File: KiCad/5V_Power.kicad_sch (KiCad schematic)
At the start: 12 parts, among them J4 USB_C_Receptacle_USB2.0_14P

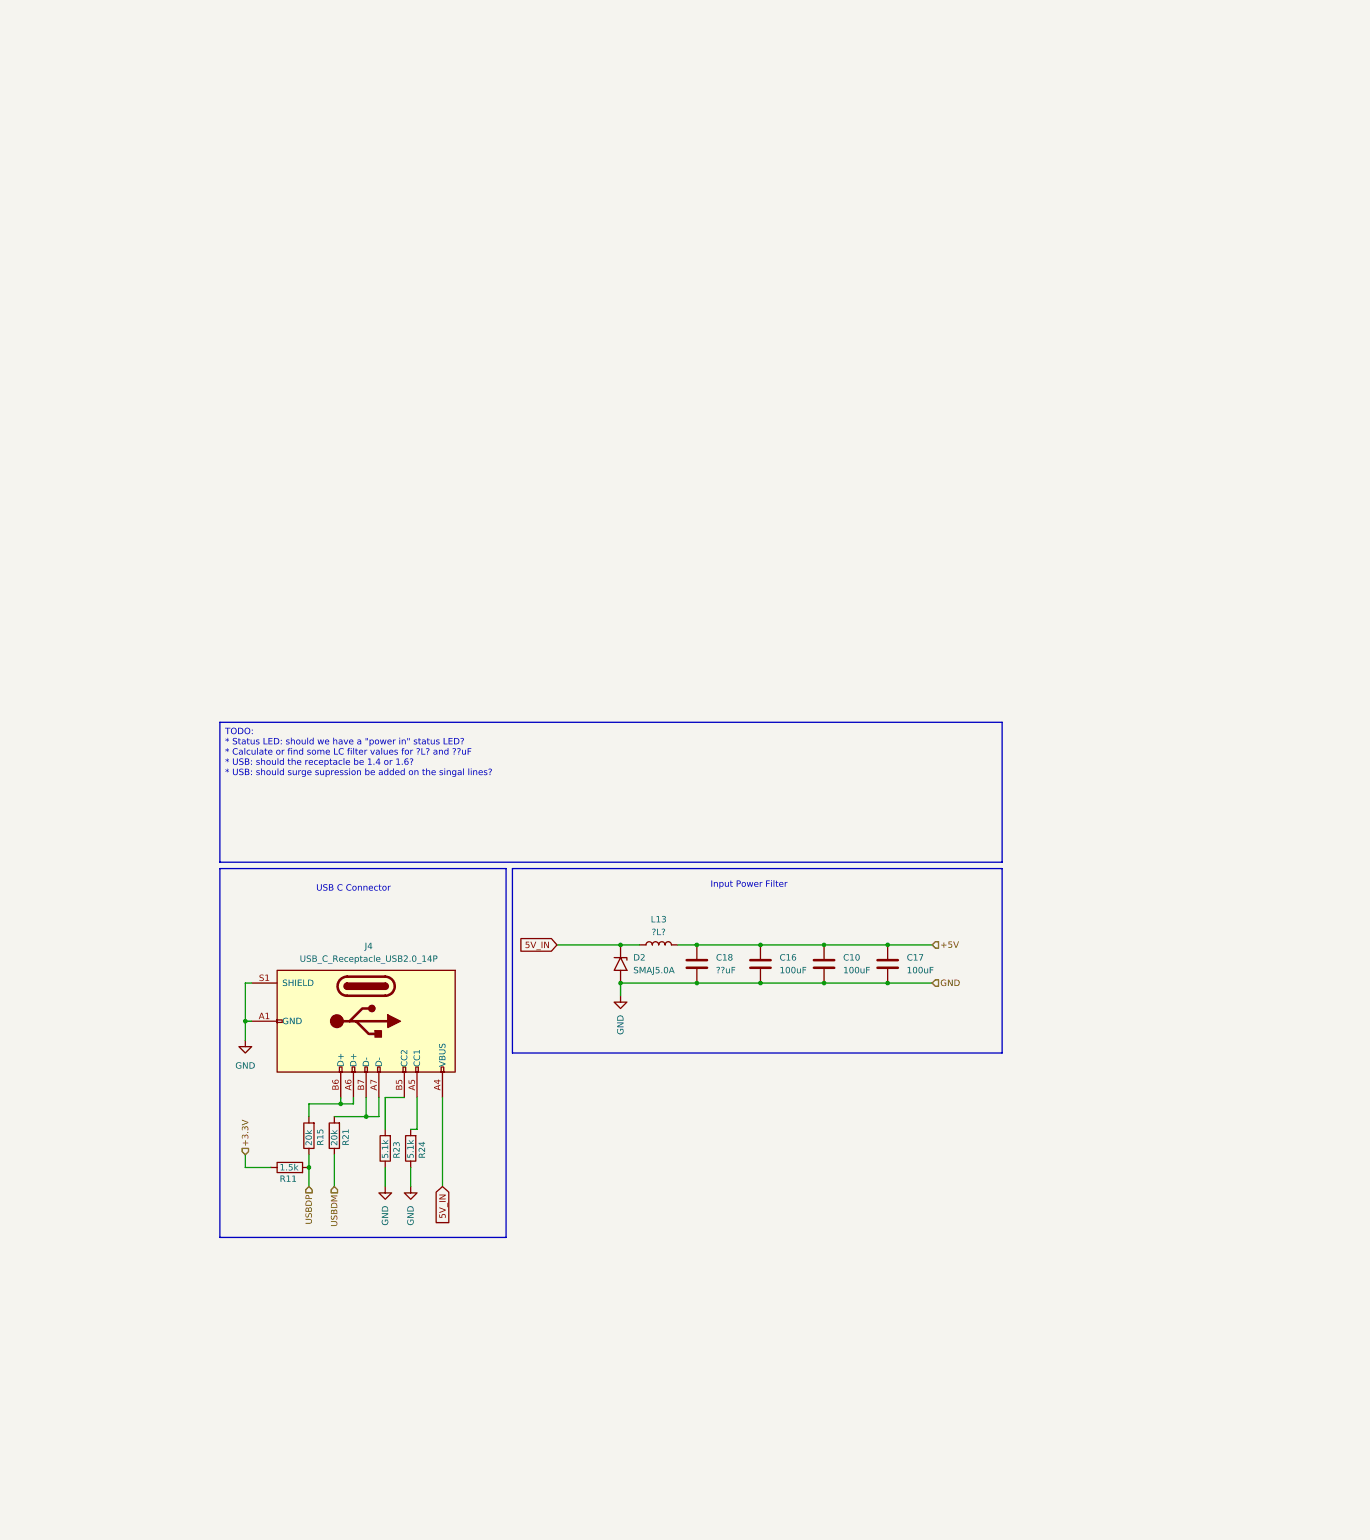
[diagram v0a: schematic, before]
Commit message: Use 12V Power
* Use 12 V Power
* Update to an F103 processor with better compatibility with Katapult
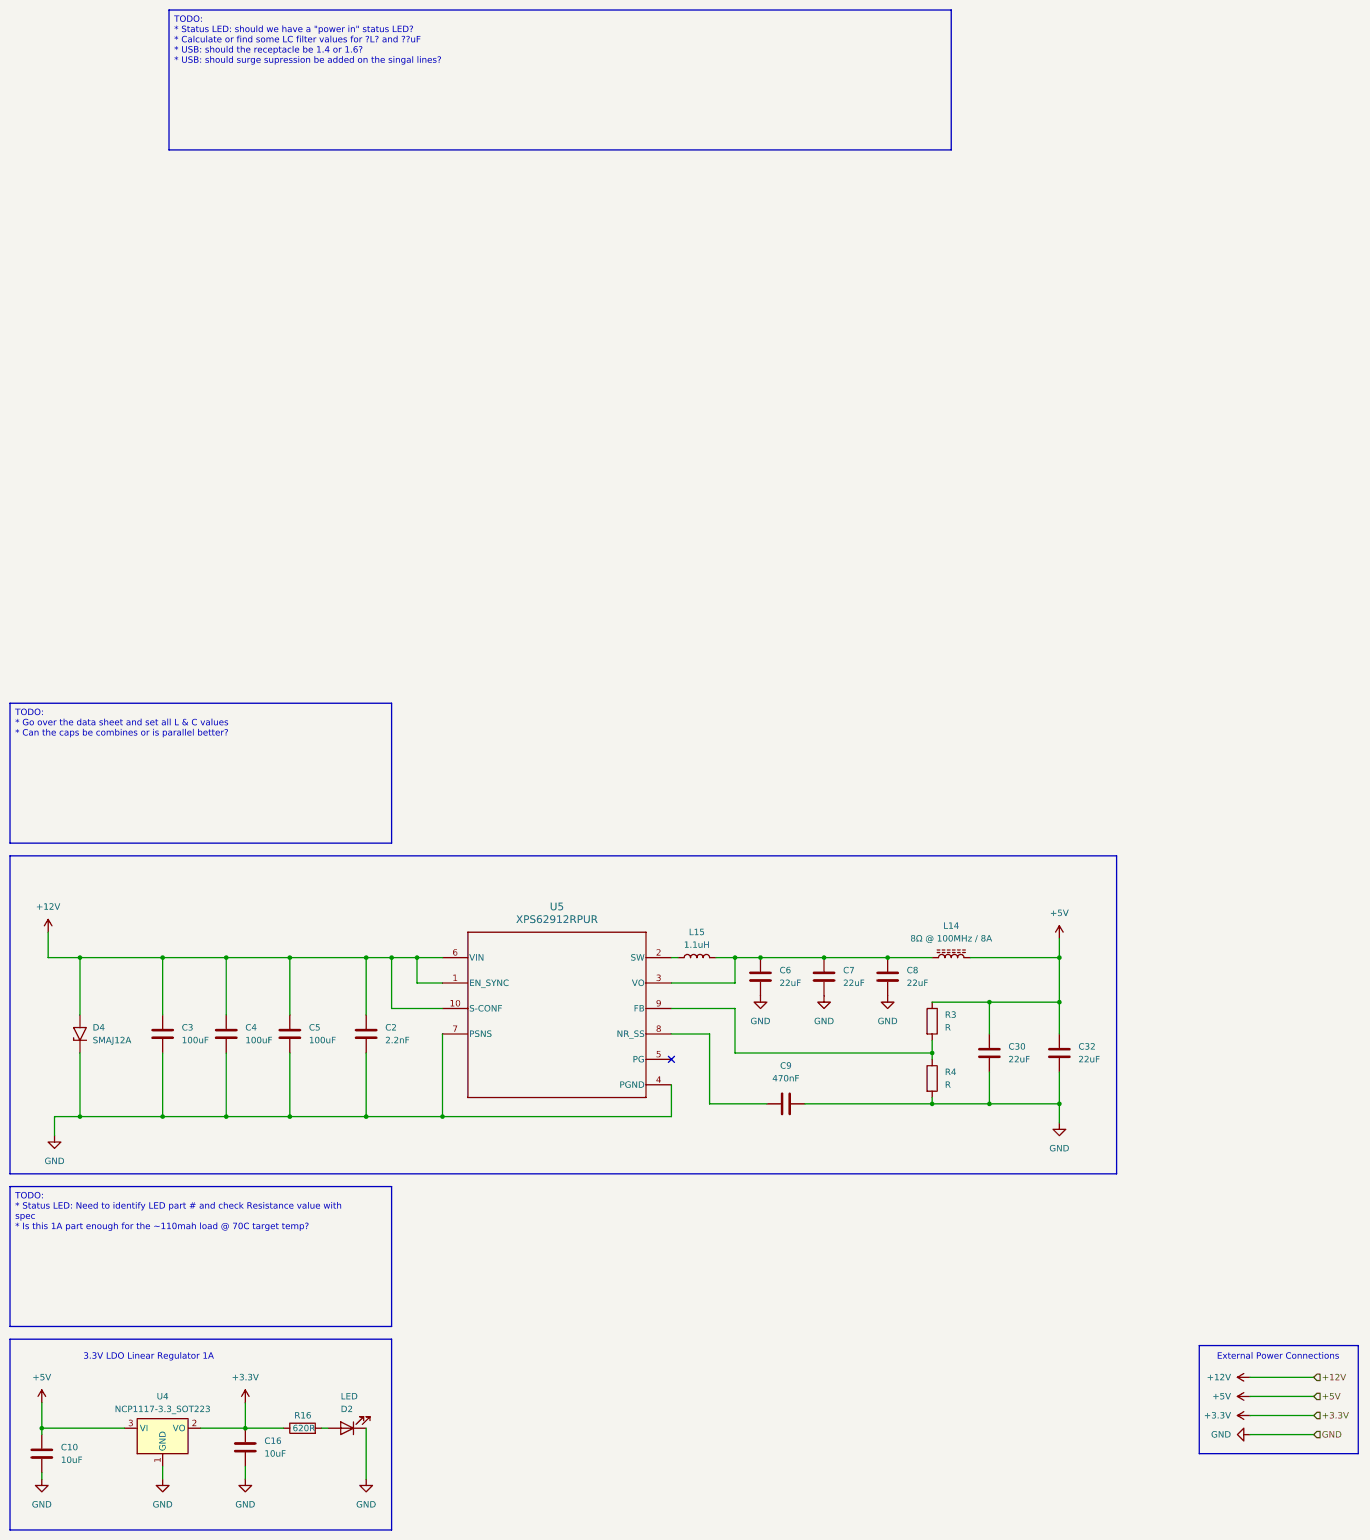
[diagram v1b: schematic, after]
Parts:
- removed C17: 100uF, symbol Device:C
- removed C18: ??uF, symbol Device:C
- removed D2: SMAJ5.0A, Diode_SMD:D_SMA, symbol Diode:SMAJ5.0A
- removed J4: USB_C_Receptacle_USB2.0_14P, symbol Connector:USB_C_Receptacle_USB2.0_14P
- removed L13: ?L?, symbol Device:L
- removed R11: 1.5k, symbol Device:R
- removed R15, R21: 20k, symbol Device:R
- removed R23, R24: 5.1k, symbol Device:R
- added C2: 2.2nF, Capacitor_SMD:C_0603_1608Metric_Pad1.08x0.95mm_HandSolder, symbol Device:C
- added C3, C4, C5: 100uF, Capacitor_SMD:C_1206_3216Metric, symbol Device:C
- added C30, C32, C6, C7, C8: 22uF, Capacitor_SMD:C_0603_1608Metric_Pad1.08x0.95mm_HandSolder, symbol Device:C
- added C9: 470nF, Capacitor_SMD:C_0603_1608Metric_Pad1.08x0.95mm_HandSolder, symbol Device:C
- added D2: LED, LED_SMD:LED_1206_3216Metric_Pad1.42x1.75mm_HandSolder, symbol Device:LED
- added D4: SMAJ12A, Diode_SMD:D_SMA, symbol Diode:SMAJ12A
- added L14: 8Ω @ 100MHz / 8A, Inductor_SMD:L_0603_1608Metric_Pad1.05x0.95mm_HandSolder, symbol Device:L_Ferrite
- added L15: 1.1uH, Capacitor_SMD:C_0603_1608Metric_Pad1.08x0.95mm_HandSolder, symbol Device:L
- added R16: 620R, Resistor_SMD:R_0603_1608Metric_Pad0.98x0.95mm_HandSolder, symbol Device:R
- added R3, R4: R, Resistor_SMD:R_0603_1608Metric_Pad0.98x0.95mm_HandSolder, symbol Device:R
- added U4: NCP1117-3.3_SOT223, Package_TO_SOT_SMD:SOT-223-3_TabPin2, symbol Regulator_Linear:NCP1117-3.3_SOT223
- added U5: XPS62912RPUR, RPU0010A-MFG, symbol TPS62912:XPS62912RPUR
- C10, C16: value 100uF -> 10uF; footprint (none) -> Capacitor_SMD:C_0603_1608Metric_Pad1.08x0.95mm_HandSolder
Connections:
- net +3.3V: now also C16.1, R16.1, U4.2 (VO)
- net +5V: now also C30.1, C32.1, L14.2, R3.1, U4.3 (VI); no longer C16.1
- net GND: now also C2.2, C3.2, C30.2, C32.2, C4.2, C5.2, C6.2, C7.2, C8.2, C9.1, D2.1 (K), D4.1 (A1), R4.2, U4.1 (GND), U5.4 (PGND), U5.7 (PSNS)
- new net: D2.2 (A), R16.2
- new net: C6.1, C7.1, C8.1, L14.1, L15.2, U5.3 (VO)
- new net: L15.1, U5.2 (SW)
- new net: C9.2, U5.8 (NR_SS)
- new net: R3.2, R4.1, U5.9 (FB)
- new net +12V: C2.1, C3.1, C4.1, C5.1, D4.2 (A2), U5.1 (EN_SYNC), U5.10 (S-CONF), U5.6 (VIN)
- no-connect marks 0 -> 1
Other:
- note added: "3.3V LDO Linear Regulator 1A"
- note added: "External Power Connections"
- note removed: "Input Power Filter"
- note removed: "USB C Connector"

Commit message: Update 5V Power Stage
* Update the 5V power stage based on the recommendations from TI.
* Updated standard passive footprint to 0805 hand solder configuration
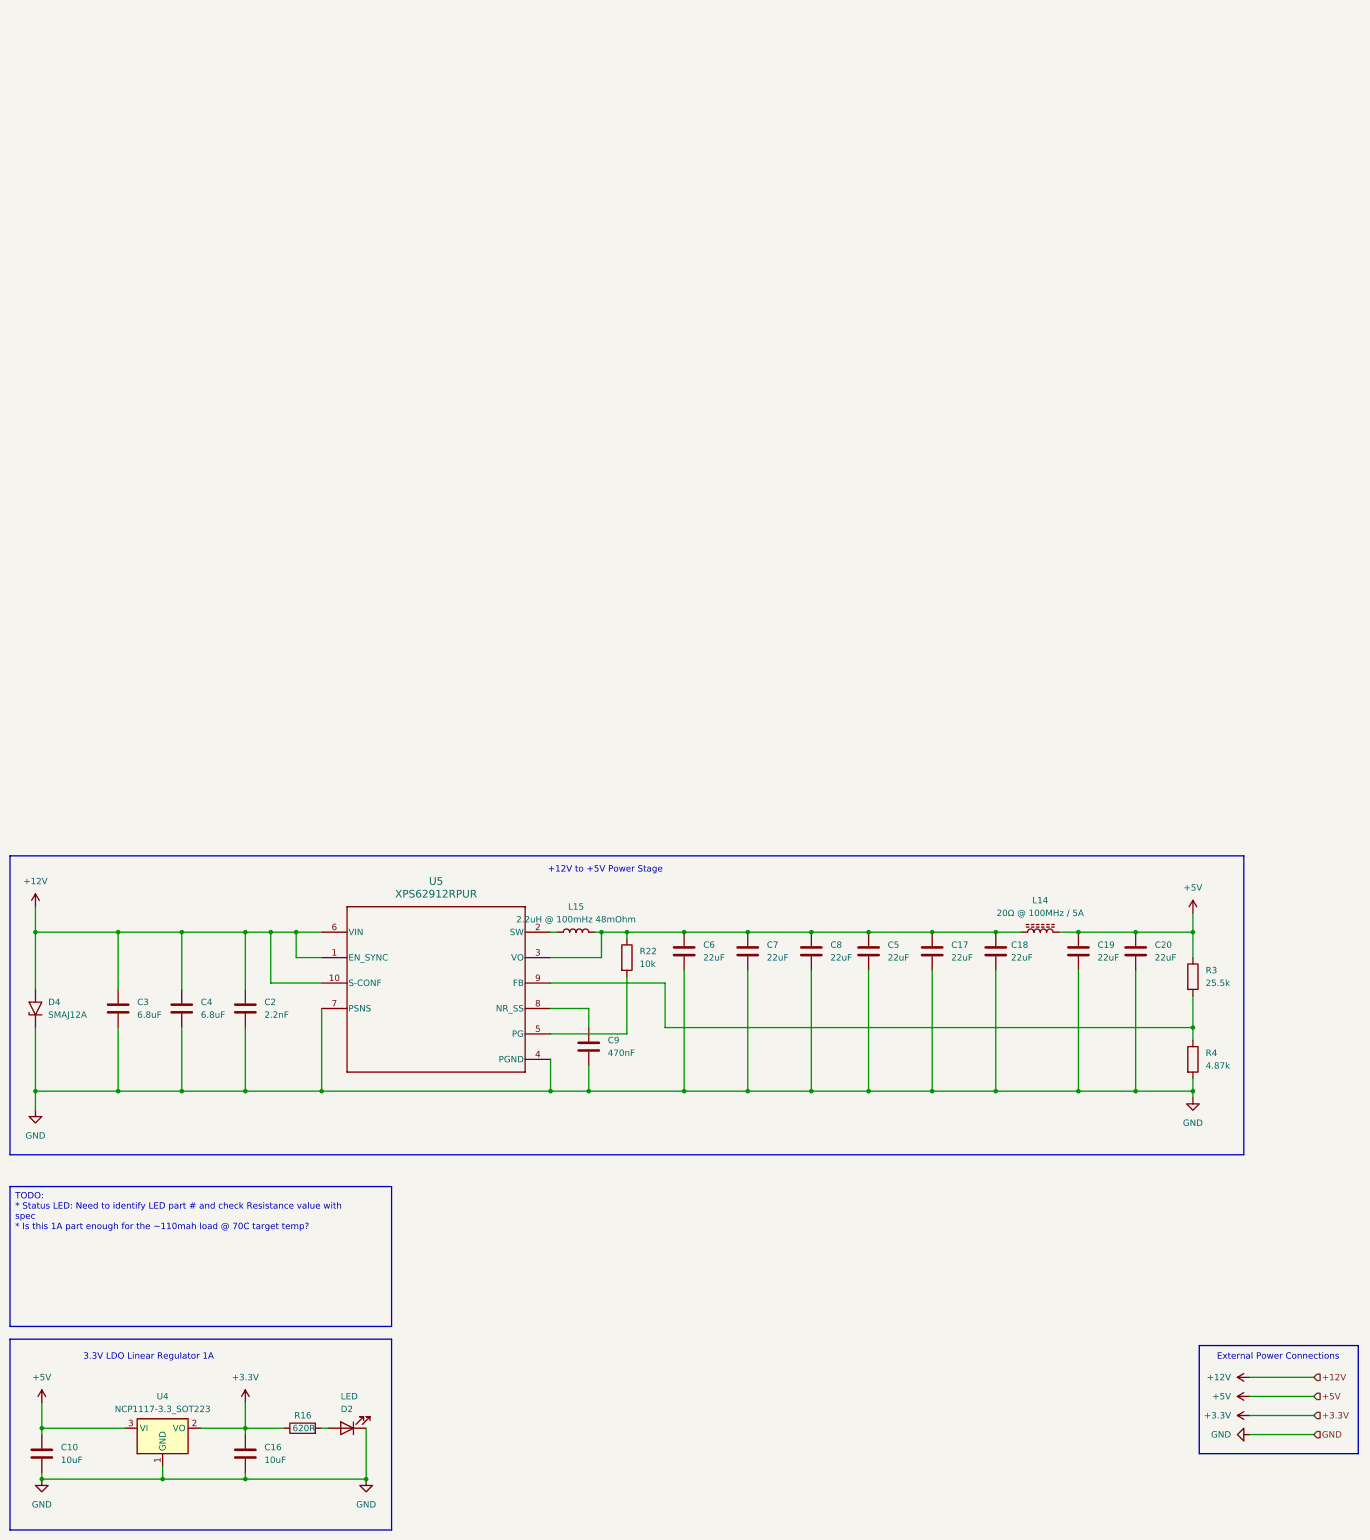
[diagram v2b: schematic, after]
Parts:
- removed C30, C32: 22uF, Capacitor_SMD:C_0603_1608Metric_Pad1.08x0.95mm_HandSolder, symbol Device:C
- added C17, C18, C19, C20: 22uF, Capacitor_SMD:C_0805_2012Metric_Pad1.18x1.45mm_HandSolder, symbol Device:C
- added R22: 10k, Resistor_SMD:R_0805_2012Metric_Pad1.20x1.40mm_HandSolder, symbol Device:R
- C10, C16, C2, C6, C7, C8, C9: footprint Capacitor_SMD:C_0603_1608Metric_Pad1.08x0.95mm_HandSolder -> Capacitor_SMD:C_0805_2012Metric_Pad1.18x1.45mm_HandSolder
- C3, C4: value 100uF -> 6.8uF; footprint Capacitor_SMD:C_1206_3216Metric -> Capacitor_SMD:C_0805_2012Metric_Pad1.18x1.45mm_HandSolder
- C5: value 100uF -> 22uF; footprint Capacitor_SMD:C_1206_3216Metric -> Capacitor_SMD:C_0805_2012Metric_Pad1.18x1.45mm_HandSolder
- L14: value 8Ω @ 100MHz / 8A -> 20Ω @ 100MHz / 5A; footprint Inductor_SMD:L_0603_1608Metric_Pad1.05x0.95mm_HandSolder -> Inductor_SMD:L_0805_2012Metric_Pad1.05x1.20mm_HandSolder
- L15: value 1.1uH -> 2.2uH @ 100mHz 48mOhm; footprint Capacitor_SMD:C_0603_1608Metric_Pad1.08x0.95mm_HandSolder -> Inductor_SMD:L_Pulse_PA4320
- R16: footprint Resistor_SMD:R_0603_1608Metric_Pad0.98x0.95mm_HandSolder -> Resistor_SMD:R_0805_2012Metric_Pad1.20x1.40mm_HandSolder
- R3: value R -> 25.5k; footprint Resistor_SMD:R_0603_1608Metric_Pad0.98x0.95mm_HandSolder -> Resistor_SMD:R_0805_2012Metric_Pad1.20x1.40mm_HandSolder
- R4: value R -> 4.87k; footprint Resistor_SMD:R_0603_1608Metric_Pad0.98x0.95mm_HandSolder -> Resistor_SMD:R_0805_2012Metric_Pad1.20x1.40mm_HandSolder
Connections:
- net +12V: no longer C5.1
- net +5V: now also C19.1, C20.1
- net GND: now also C17.2, C18.2, C19.2, C20.2
- net at C6.1, C7.1, C8.1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: now also C5.1, C17.1, C18.1, R22.1
- net at U5.5 (PG): now also R22.2
- no-connect marks 1 -> 0
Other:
- note added: "+12V to +5V Power Stage"
- moved on the sheet: C16, C2, C3, C4, C6, C7, C8, D4, L14, L15, R3, R4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
